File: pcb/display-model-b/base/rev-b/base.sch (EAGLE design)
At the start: 48 parts, among them J1 SNG-2MM-HEADER-07-V, Q1 MMBT3904, U1 TSL2561FN, U2 PCA9634PW, U3 74AHC1G04DCK, U4 AP5724W, U5 74AHC1G04DCK, U6 AP5724W, U7 74AHC1G04DCK, U8 AP5724W, U9 74AHC1G04DCK, X1 CLOCK_LED_SEGMENT, X2 CLOCK_LED_SEGMENT, X3 CLOCK_LED_SEGMENT, X4 CLOCK_LED_SEGMENT, X5 CLOCK_LED_DOTS

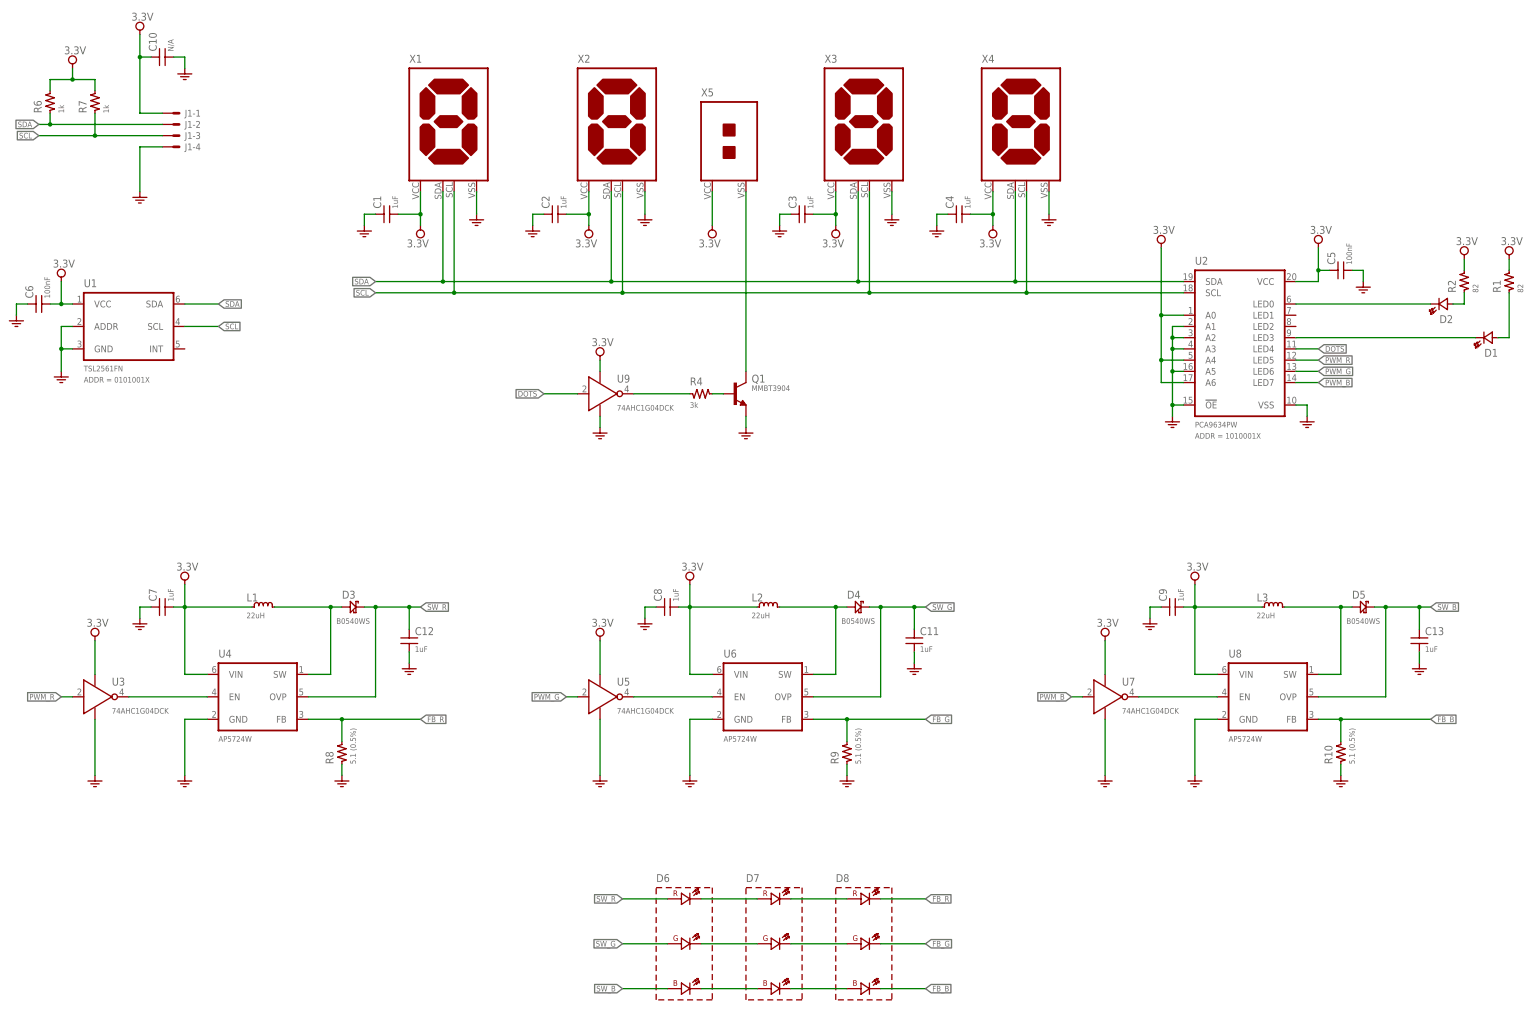
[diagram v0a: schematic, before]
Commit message: Display base pcb (rev C), Touch panel (rev B)
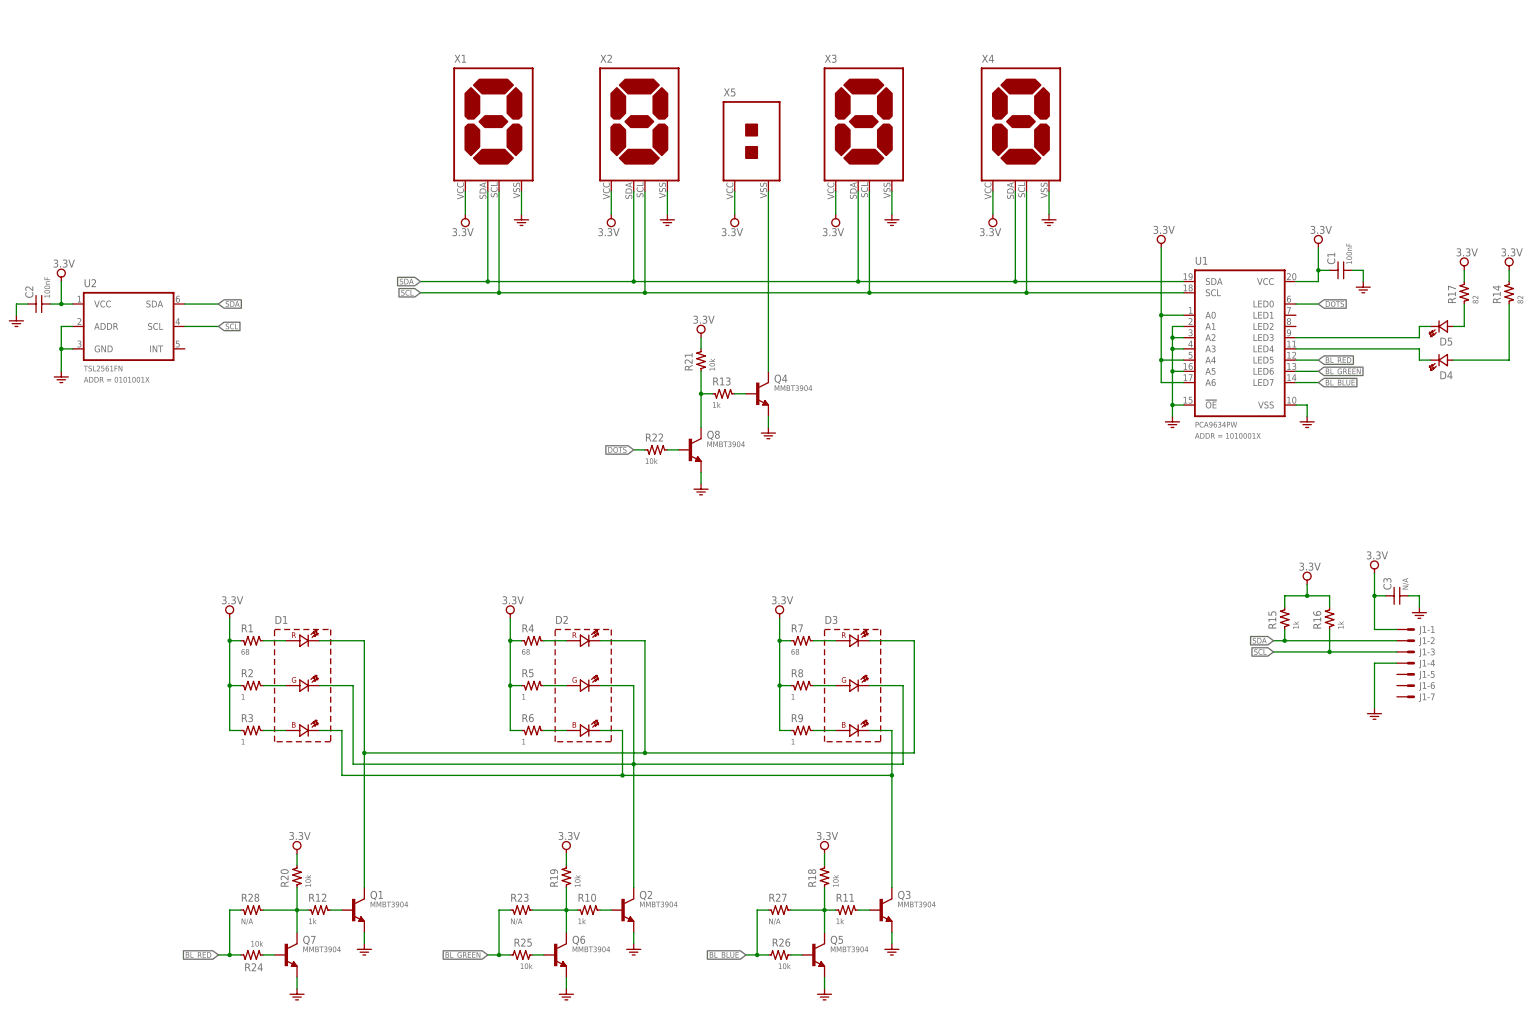
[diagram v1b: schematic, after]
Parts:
- removed C10: N/A, Passive:CAP-0805
- removed C11, C12, C13, C4, C7, C8, C9: 1uF, Passive:CAP-0603
- removed C5, C6: 100nF, Passive:CAP-0603
- removed D6, D7, D8: SMP6-RGB, Optoelectronic:SMP6-RGB
- removed L1, L2, L3: 22uH, Passive:IND-4X4
- removed U3, U5, U7, U9: 74AHC1G04DCK, Logic:74AHC1G04DCK
- removed U4, U6, U8: AP5724W, IC:AP5724W
- added Q2, Q3, Q4, Q5, Q6, Q7, Q8: MMBT3904, Transistor:MMBT3904
- added R11, R12, R13, R15, R16: 1k, Passive:RES-0603
- added R14, R17: 82, Passive:RES-0603
- added R18, R19, R20, R21, R22, R24, R25, R26: 10k, Passive:RES-0603
- added R23, R27, R28: N/A, Passive:RES-0603
- added R3, R5: 1, Passive:RES-0603
- C1, C2: value 1uF -> 100nF; DESCRIPTION {DESCRIPTION} - SMT 0603 - {value} -> (none); PACKAGE SMT 0603 -> (none)
- C3: value 1uF -> N/A; device Passive:CAP-0603 -> Passive:CAP-0805; DESCRIPTION {DESCRIPTION} - SMT 0603 - {value} -> {DESCRIPTION} - SMT 0805 - {value}; PACKAGE SMT 0603 -> SMT 0805
- D1: value {ATTR:COLOR} -> SMP6-RGB; device Optoelectronic:LED-T1 -> Optoelectronic:SMP6-RGB; COLOR Green -> (none); DESCRIPTION {DESCRIPTION} T1 (3mm) - {ATTR:COLOR} -> (none); MFG (none) -> BIVAR; PACKAGE T1 -> (none); SKU - -> SMP6-RGB; VALUE {ATTR:COLOR} -> (none)
- D2: value {ATTR:COLOR} -> SMP6-RGB; device Optoelectronic:LED-T1 -> Optoelectronic:SMP6-RGB
- D3: value (none) -> SMP6-RGB; device Passive:DIODE_SCHOTTKY-SOD323 -> Optoelectronic:SMP6-RGB; PART_NO B0540WS -> (none)
- D4: value (none) -> {ATTR:COLOR}; device Passive:DIODE_SCHOTTKY-SOD323 -> Optoelectronic:LED-T1; PART_NO B0540WS -> (none)
- D5: value (none) -> {ATTR:COLOR}; device Passive:DIODE_SCHOTTKY-SOD323 -> Optoelectronic:LED-T1; COLOR (none) -> Green; DESCRIPTION (none) -> {DESCRIPTION} T1 (3mm) - {ATTR:COLOR}; PACKAGE (none) -> T1; PART_NO B0540WS -> (none); SKU (none) -> -; VALUE (none) -> {ATTR:COLOR}
- R1: value 82 -> 68; DESCRIPTION {DESCRIPTION} - SMT 0603 - {VALUE} -> (none); PACKAGE SMT 0603 -> (none)
- R10: value 5.1 (0.5%) -> 1k; DESCRIPTION {DESCRIPTION} - SMT 0603 - {VALUE} -> (none); PACKAGE SMT 0603 -> (none)
- R2: value 82 -> 1; DESCRIPTION (none) -> {DESCRIPTION} - SMT 0603 - {VALUE}; PACKAGE (none) -> SMT 0603
- R4: value 3k -> 68; DESCRIPTION {DESCRIPTION} - SMT 0603 - {VALUE} -> (none); PACKAGE SMT 0603 -> (none)
- R6: value 1k -> 1; DESCRIPTION (none) -> {DESCRIPTION} - SMT 0603 - {VALUE}; PACKAGE (none) -> SMT 0603
- R7: value 1k -> 68
- R8: value 5.1 (0.5%) -> 1
- R9: value 5.1 (0.5%) -> 1; DESCRIPTION (none) -> {DESCRIPTION} - SMT 0603 - {VALUE}; PACKAGE (none) -> SMT 0603
- U1: value TSL2561FN -> PCA9634PW; device Optoelectronic:TSL2561FN -> IC:PCA9634PW; ADDR 0101001X -> 1010001X
- U2: value PCA9634PW -> TSL2561FN; device IC:PCA9634PW -> Optoelectronic:TSL2561FN; ADDR 1010001X -> 0101001X
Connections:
- removed net FB_B: D8.BK, R10.2, U8.FB
- removed net FB_G: D8.GK, R9.2, U6.FB
- removed net FB_R: D8.RK, R8.2, U4.FB
- removed net N$29: U7.Y, U8.EN
- removed net PWM_B: U2.LED7, U7.A
- removed net PWM_G: U2.LED6, U5.A
- removed net PWM_R: U2.LED5, U3.A
- removed net SW_B: C13.1, D5.K, D6.BA, U8.OVP
- removed net SW_G: C11.1, D4.K, D6.GA, U6.OVP
- removed net SW_R: C12.1, D3.K, D6.RA, U4.OVP
- new net BL_BLUE: R26.2, R27.1, U1.LED7
- new net BL_GREEN: R23.1, R25.2, U1.LED6
- new net BL_RED: R24.2, R28.1, U1.LED5
- new net N$11: D3.RA, R7.2
- new net N$13: Q2.B, R10.2
- new net N$14: Q3.B, R11.2
- new net N$17: Q1.B, R12.2
- new net N$22: Q6.C, R10.1, R19.1, R23.2
- new net N$23: Q5.C, R11.1, R18.1, R27.2
- new net N$24: Q7.C, R12.1, R20.1, R28.2
- new net N$27: Q8.B, R22.2
- new net N$30: Q7.B, R24.1
- new net N$7: D2.GA, R5.2
- new net N$9: D3.BA, R9.2
- net 3.3V: now also C1.1, C3.1, R1.1, R14.2, R15.2, R16.2, R17.2, R18.2, R19.2, R2.1, R20.2, R21.2, R3.1, R4.1, R5.1, R6.1, R7.1, R8.1, R9.1, U1.A0, U1.A4, U1.A6; no longer C1.2, C10.1, C3.2, C4.2, C5.1, C6.2, C7.2, C8.2, C9.2, L1.1, L2.1, L3.1, R1.2, R2.2, R6.2, R7.2, U2.A0, U2.A4, U2.A6, U3.VCC, U4.VIN, U5.VCC, U6.VIN, U7.VCC, U8.VIN, U9.VCC
- net DOTS: now also R22.1, U1.LED0; no longer U2.LED4, U9.A
- net GND: now also C1.2, C3.2, Q2.E, Q3.E, Q4.E, Q5.E, Q6.E, Q7.E, Q8.E, U1.!OE, U1.A1, U1.A2, U1.A3, U1.A5, U1.VSS, U2.ADDR, U2.GND; no longer C1.1, C10.2, C11.2, C12.2, C13.2, C3.1, C4.1, C5.2, C6.1, C7.1, C8.1, C9.1, R10.1, R8.1, R9.1, U1.ADDR, U1.GND, U2.!OE, U2.A1, U2.A2, U2.A3, U2.A5, U2.VSS, U3.GND, U4.GND, U5.GND, U6.GND, U7.GND, U8.GND, U9.GND
- net N$1: now also D1.GA, R2.2; no longer D6.RK, D7.RA
- net N$10: now also D3.GA, R8.2; no longer D4.A, L2.2, U6.SW
- net N$12: now also D1.RK, D2.RK, D3.RK, Q1.C; no longer D5.A, L3.2, U8.SW
- net N$15: now also Q4.C; no longer Q1.C
- net N$16: now also Q4.B, R13.2; no longer Q1.B, R4.2
- net N$18: now also D4.K, U1.LED4; no longer D2.K, U2.LED0
- net N$19: now also D4.A, R14.1; no longer D2.A, R2.1
- net N$2: now also D1.RA, R1.2; no longer D7.RK, D8.RA
- net N$20: now also D5.A, R17.1; no longer D1.A, R1.1
- net N$21: now also D5.K, U1.LED3; no longer D1.K, U2.LED3
- net N$25: now also Q5.B, R26.1; no longer U3.Y, U4.EN
- net N$26: now also Q8.C, R13.1, R21.1; no longer R4.1, U9.Y
- net N$28: now also Q6.B, R25.1; no longer U5.Y, U6.EN
- net N$3: now also D1.BA, R3.2; no longer D7.GK, D8.GA
- net N$4: now also D2.RA, R4.2; no longer D6.GK, D7.GA
- net N$5: now also D1.GK, D2.GK, D3.GK, Q2.C; no longer D6.BK, D7.BA
- net N$6: now also D1.BK, D2.BK, D3.BK, Q3.C; no longer D7.BK, D8.BA
- net N$8: now also D2.BA, R6.2; no longer D3.A, L1.2, U4.SW
- net SCL: now also R16.1; no longer R7.1
- net SDA: now also R15.1; no longer R6.1
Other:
- moved on the sheet: C1, C2, C3, J1-1, J1-2, J1-3, J1-4, Q1, R1, R10, R2, R4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
